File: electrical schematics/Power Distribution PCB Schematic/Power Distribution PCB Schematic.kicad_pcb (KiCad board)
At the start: 2 copper layers, 100 x 100 mm, 59 parts, among them J1 XT60_Port, J10 BDC_Motor_Screw_Terminal, J11 BDC_Motor_Screw_Terminal, J12 Encoder_Header, J13 Encoder_Header, J14 Encoder_Header, J15 Encoder_Header, J16 6V_to_Motors_Screw, J2 12V_6V_Input_Screw, J20 5V_Regulator_Header, J21 GPS_Module_Header, J3 6V_Output_Screw, J4 IMU_Module_Header, J5 Magnetometer_Module_Header, J6 Raspberry_Pi_4, J7 Servo_PWM_Header, J8 BDC_Motor_Screw_Terminal, J9 BDC_Motor_Screw_Terminal

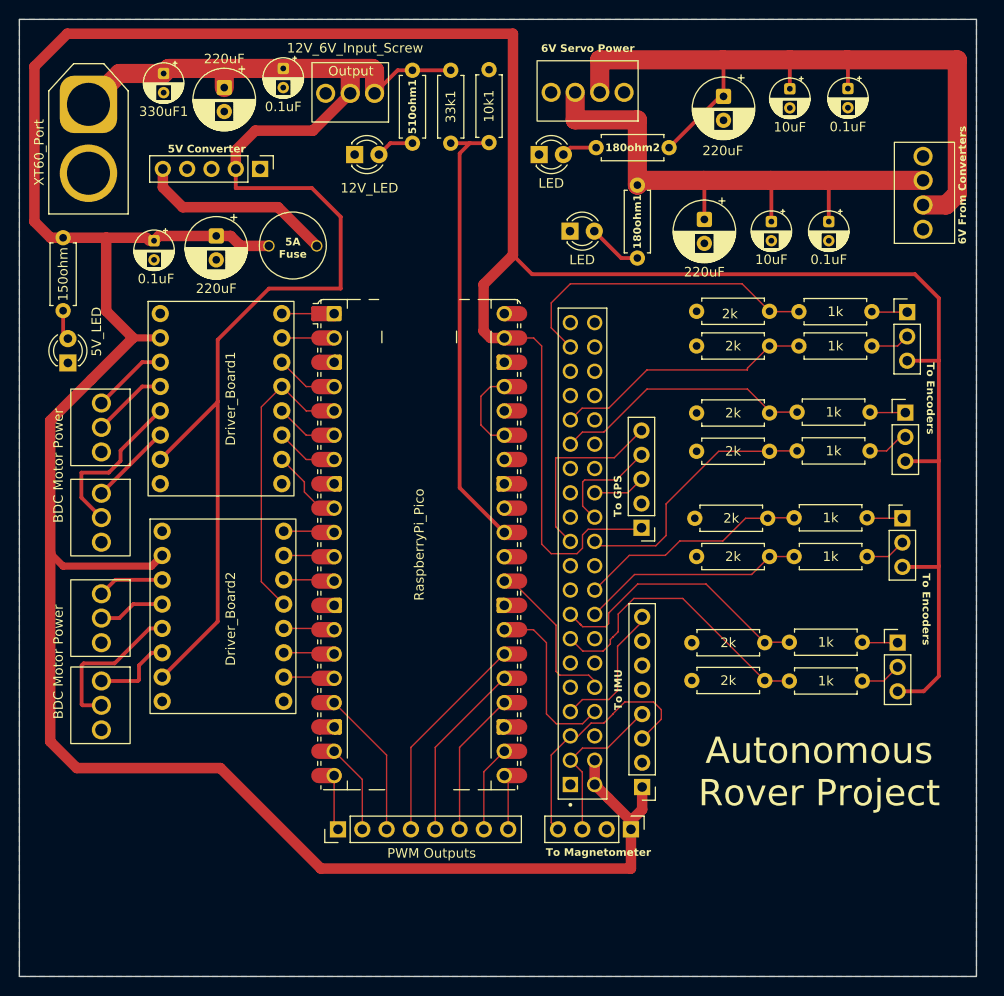
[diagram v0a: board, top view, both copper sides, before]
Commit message: Electrical System Modifications
Forgot about the ultrasonic sensor, added to PCB schematic + layout
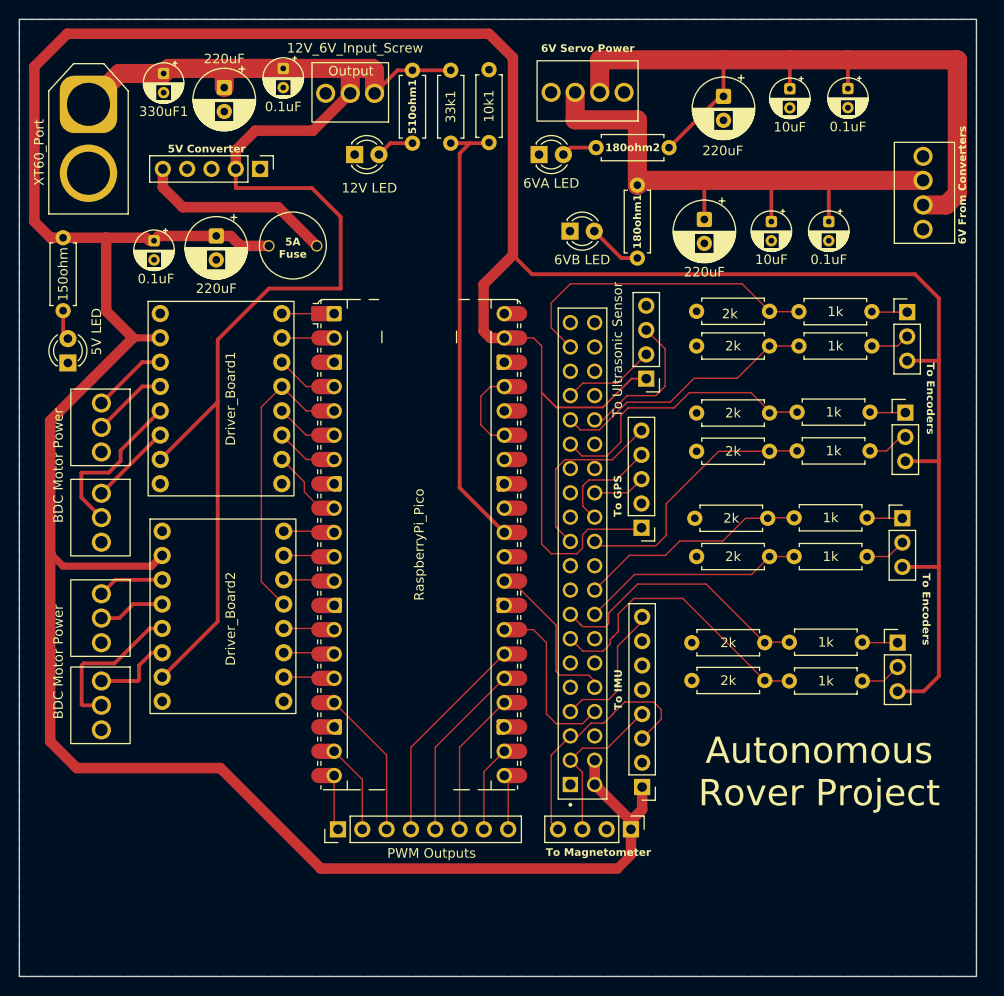
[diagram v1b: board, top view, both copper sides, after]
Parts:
- added J17: Ultrasonic_Sensor_Header, Connector_PinHeader_2.54mm:PinHeader_1x04_P2.54mm_Vertical, F.Cu at (85.5, 63.0)
- D3: value LED -> 6VB LED
- D4: value LED -> 6VA LED
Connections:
- J6 pad 32: unconnected-(J6-GPIO12/PWM0-Pad32) -> Net-(J17-Echo)
- J6 pad 33: unconnected-(J6-GPIO13/PWM1-Pad33) -> Net-(J17-Trig)
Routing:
- net Net-(J17-Echo): track 0.00 -> 15.5 mm
- net /5V_Bus: track 423.6 -> 434.2 mm
- net Net-(J17-Trig): track 0.00 -> 9.71 mm
- net Net-(J6-GPCLK1/GPIO05): track 27.3 -> 29.6 mm
- net Net-(J6-GPCLK2/GPIO06): track 27.2 -> 27.9 mm
- net Net-(J21-PPS): track 19.5 -> 18.8 mm
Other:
- board text added: "12V LED"
- board text added: "5V LED"
- board text added: "To Ultrasonic Sensor"
- board text removed: "12V_LED"
- board text removed: "5V_LED"

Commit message: PCB Layout Adjustments + Drivetrain Design
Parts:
- D3: value 6VB LED -> LED
- D4: value 6VA LED -> LED
- moved D3 2.74 mm to (80.3, 47.6), turned to 180 degrees
- moved D4 2.47 mm to (76.8, 39.6), turned to 180 degrees
- moved D2 2.40 mm to (25.1, 59.0), turned to -90 degrees
- moved D1 2.24 mm to (57.3, 39.6), turned to 180 degrees
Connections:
- D1 pad 1: GND -> Net-(D1-A)
- D1 pad 2: Net-(D1-A) -> GND
- D2 pad 1: GND -> Net-(D2-A)
- D2 pad 2: Net-(D2-A) -> GND
- D3 pad 1: GND -> Net-(D3-A)
- D3 pad 2: Net-(D3-A) -> GND
- D4 pad 1: GND -> Net-(D4-A)
- D4 pad 2: Net-(D4-A) -> GND
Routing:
- net /12V_Bus: track 150.9 -> 149.9 mm

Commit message: PCB Schematic v2
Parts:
- removed 180ohm1, 180ohm2: R_US, Resistor_THT:R_Axial_DIN0207_L6.3mm_D2.5mm_P7.62mm_Horizontal
- removed C10, C9: 220uF, Capacitor_THT:CP_Radial_D6.3mm_P2.50mm
- removed C5, C6: 10uF, Capacitor_THT:CP_Radial_D4.0mm_P2.00mm
- removed C7, C8: 0.1uF, Capacitor_THT:CP_Radial_D4.0mm_P2.00mm
- removed D3, D4: LED, LED_THT:LED_D3.0mm
- removed the J16 at (84.7, 29.8)
- removed the J2 at (58.6, 30.0)
- removed the J3 at (117.7, 48.9)
- added REF**: MountingHole_3.2mm_M3, MountingHole:MountingHole_3.2mm_M3, F.Cu at (116.0, 121.5)
- added REF**: MountingHole_3.2mm_M3, MountingHole:MountingHole_3.2mm_M3, F.Cu at (116.0, 29.5)
- added REF**: MountingHole_3.2mm_M3, MountingHole:MountingHole_3.2mm_M3, F.Cu at (24.0, 29.5)
- added REF**: MountingHole_3.2mm_M3, MountingHole:MountingHole_3.2mm_M3, F.Cu at (24.0, 121.5)
- added To_6VA_Conv1: To_6VA_Converter, Rover_Project_2:12AWG Screw Terminal, F.Cu at (60.0, 32.6)
- added To_6VB_Conv1: To_6VB_Convertor, Rover_Project_2:12AWG Screw Terminal, F.Cu at (77.5, 32.6)
- 330uF1, C1, C4: footprint Capacitor_THT:CP_Radial_D4.0mm_P2.00mm -> Rover_Project_2:Ceramic Cap
- Driver_Board1, Driver_Board2: footprint Rover_Project.:Motor Driver Board -> Rover_Project_2:Motor Driver Board
- F1: footprint Rover_Project.:Fuse_TH_5A -> Rover_Project_2:Fuse_TH_5A
- J10: renamed from J9; footprint Rover_Project.:01x03_Screw_Terminal -> Rover_Project_2:01x03_Screw_Terminal
- J11: renamed from J10; footprint Rover_Project.:01x03_Screw_Terminal -> Rover_Project_2:01x03_Screw_Terminal
- J12: renamed from J11; footprint Rover_Project.:01x03_Screw_Terminal -> Rover_Project_2:01x03_Screw_Terminal
- J7: renamed from J6; footprint Rover_Project.:SULLINS_PPTC202LFBN-RC -> Rover_Project_2:SULLINS_PPTC202LFBN-RC
- J9: renamed from J8; footprint Rover_Project.:01x03_Screw_Terminal -> Rover_Project_2:01x03_Screw_Terminal
- moved 10k1 28.5 mm to (97.5, 36.3)
- moved 33k1 25.0 mm to (90.0, 36.3)
- moved J13 19.8 mm to (117.2, 36.8)
- moved R13 19.4 mm to (104.6, 36.9)
- moved R14 19.4 mm to (104.6, 40.5)
- moved R4 18.0 mm to (104.7, 53.8), turned to 0 degrees
- moved J3 16.3 mm to (97.1, 94.8)
- moved D1 16.1 mm to (72.5, 45.0), turned to 0 degrees
- moved J5 16.0 mm to (97.3, 52.2)
- moved J7 16.0 mm to (88.8, 68.8)
- moved R2 15.8 mm to (104.5, 45.1), turned to 0 degrees
- moved J4 15.2 mm to (97.2, 69.6)
- moved C1 15.1 mm to (32.5, 32.0), turned to 90 degrees
- moved Driver_Board2 15.1 mm to (37.8, 112.5)
- moved D2 15.0 mm to (40.0, 60.0)
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- renumbered J12 to J13, J13 to J14, J14 to J15, J15 to J16, J5 to J2, J4 to J3, J21 to J4, J17 to J5, J20 to J6, J7 to J8
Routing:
- net /6V_A: track 76.7 -> 0.00 mm
- net /12V_Bus: track 149.9 -> 221.7 mm
- net /5V_Bus: track 434.2 -> 370.1 mm
- net /6V_B: track 59.3 -> 0.00 mm
- net Net-(J7-GPIO23/SDIO_CMD): track 23.3 -> 40.1 mm
- net Net-(J4-TXD): track 5.48 -> 18.5 mm
- net Net-(J7-GPIO27/SDIO_DAT3): track 30.6 -> 43.6 mm
- net Net-(A1-GPIO26_ADC0): track 47.1 -> 58.6 mm
- net Net-(J7-GPIO22/SDIO_CLK): track 28.5 -> 39.9 mm
- net Net-(A1-GPIO10): track 5.32 -> 15.8 mm
- net Net-(A1-GPIO9): track 5.32 -> 15.8 mm
- net Net-(A1-GPIO12): track 5.32 -> 15.8 mm
- net Net-(A1-GPIO8): track 5.32 -> 15.6 mm
- net Net-(A1-GPIO7): track 5.32 -> 15.6 mm
- net Net-(A1-GPIO11): track 5.32 -> 15.3 mm
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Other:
- board text added: "Raspberry Pi Pico"
- board text added: "To 6VA Converter"
- board text added: "To 6VB Converter"
- board text removed: "6V From Converters"
- board text removed: "6V Servo Power"
- board text removed: "Output"
